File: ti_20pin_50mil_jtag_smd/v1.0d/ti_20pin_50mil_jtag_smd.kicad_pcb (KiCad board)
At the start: 2 copper layers, 7.8 x 12.8 mm, 10 parts, among them P1 CONN_02X10, X1 JTAG-10

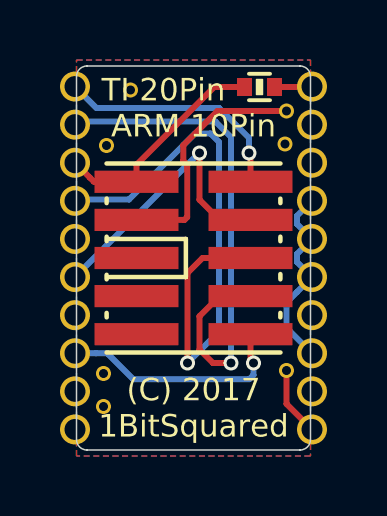
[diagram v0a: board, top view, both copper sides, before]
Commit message: Added pin 1 indicator to the smd footprint.
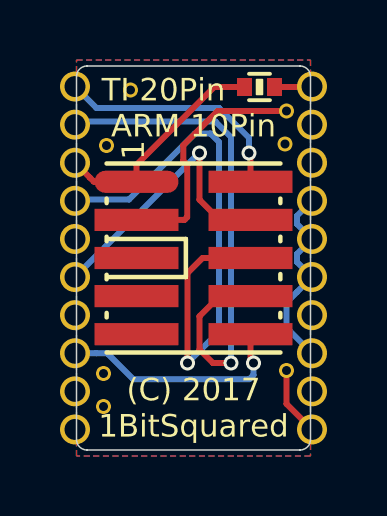
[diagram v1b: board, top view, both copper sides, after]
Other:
- board text added: "1"
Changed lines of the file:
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@@
-(kicad_pcb (version 4) (host pcbnew 4.0.5-e0-6337~49~ubuntu16.04.1)
+(kicad_pcb (version 4) (host pcbnew 4.0.6-e0-6349~53~ubuntu16.04.1)
   (general
-    (links 23)
-    (no_connects 3)
-    (area 146.074999 93.574999 153.925001 106.425001)
+    (links 0)
+    (no_connects 0)
+    (area 144.976667 91.535 155.023334 108.565)
     (thickness 1.6)
-    (drawings 11)
+    (drawings 12)
     (tracks 79)
     (zones 0)
@@
     (mod_text_size 1 1)
     (mod_text_width 0.15)
-    (pad_size 0.5 0.5)
-    (pad_drill 0.3)
+    (pad_size 0.74 2.8)
+    (pad_drill 0)
     (pad_to_mask_clearance 0.05)
     (aux_axis_origin 0 0)
@@
     (fp_line (start 3.15 2.9) (end 3.15 -2.9) (layer F.SilkS) (width 0.15))
     (fp_line (start -3.15 2.9) (end -3.15 -2.9) (layer F.SilkS) (width 0.15))
-    (pad 1 smd rect (at 2.54 -1.9 270) (size 0.74 2.8) (layers F.Cu F.Paste F.Mask)
+    (pad 1 smd oval (at 2.54 -1.9 270) (size 0.74 2.8) (layers F.Cu F.Paste F.Mask)
       (net 3 /VREF))
     (pad 2 smd rect (at 2.54 1.9 270) (size 0.74 2.8) (layers F.Cu F.Paste F.Mask)
@@
     )
   )
+  (gr_text 1 (at 148 96.4 90) (layer F.SilkS)
+    (effects (font (size 0.75 0.75) (thickness 0.1875)))
+  )
   (gr_text "(C) 2017\n1BitSquared" (at 150 105) (layer F.SilkS)
